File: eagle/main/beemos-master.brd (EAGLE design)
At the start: 99.1 x 73.7 mm, 50 parts, among them CON1 BAT, CON2 JACK_DC_BARREL, CON3 SPI, IC1 32U4, IC2 MCP73831T, IC3 MCP1703CB, IC4 DMP1045U, J1 RJ123.3, J10 RJ12STRAIGHT-I2C, J2 RJ123.3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

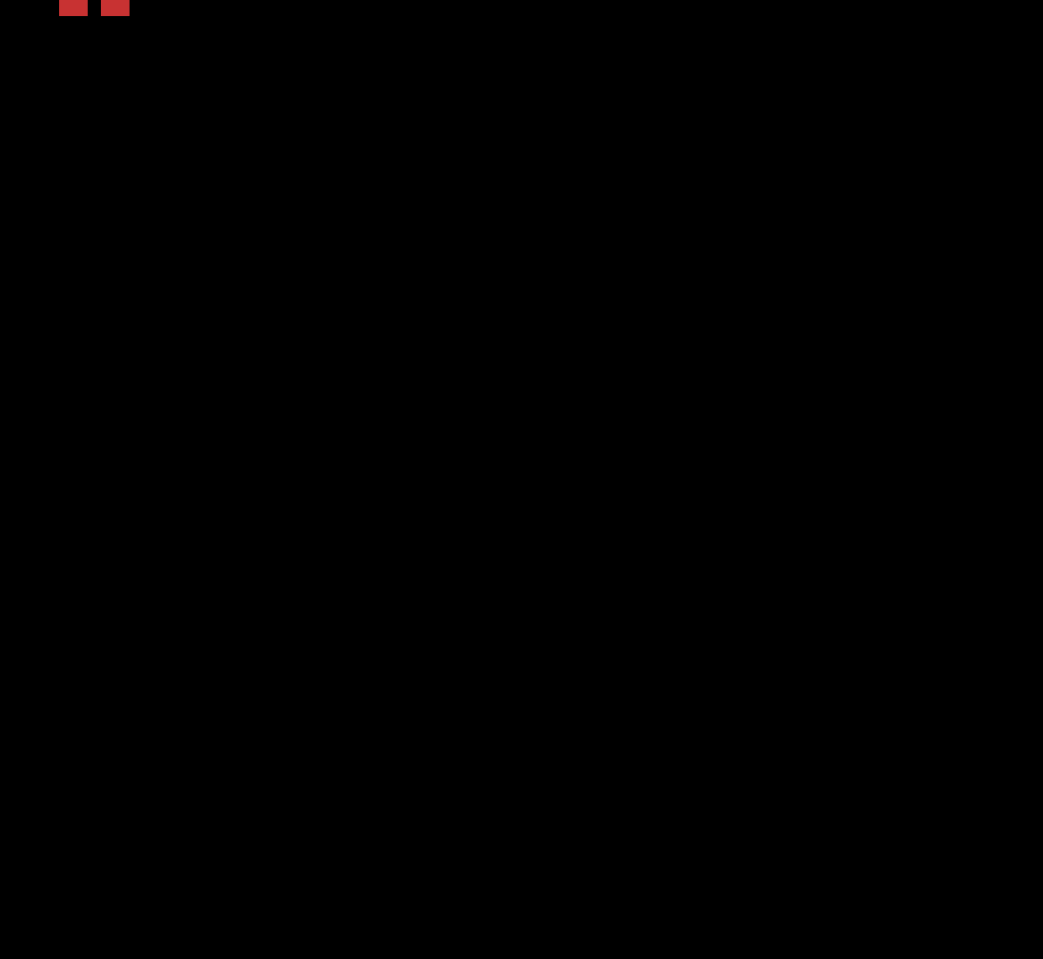
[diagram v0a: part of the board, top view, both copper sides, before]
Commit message: Added modules to schematics
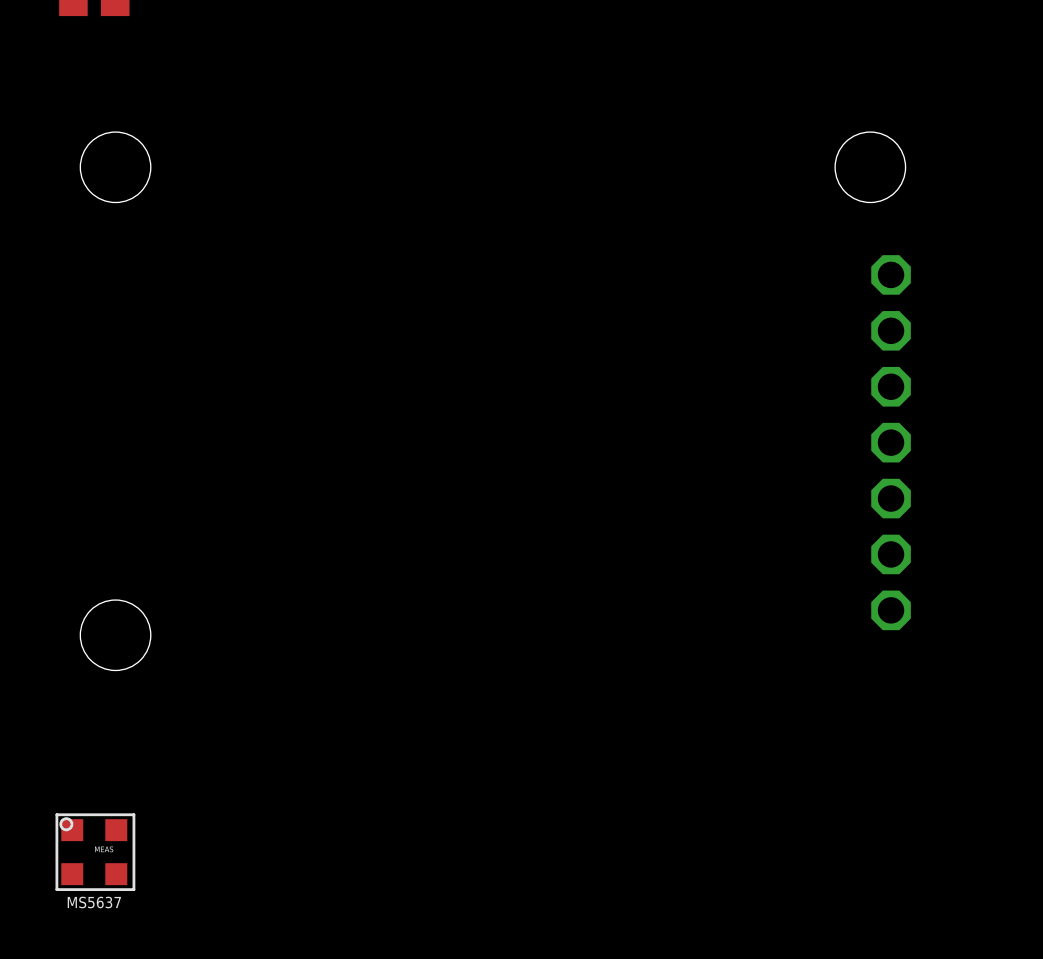
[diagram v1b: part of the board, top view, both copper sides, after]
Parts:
- added U$6: SIM800L, SIM800L:SIP
- added U$7: MS5637, MS5637:MS5637
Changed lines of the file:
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@@
 <attribute name="LCSC" value="C17561" x="15.875" y="38.735" size="1.778" layer="27" rot="R180" display="off"/>
 <attribute name="NAME" x="13.094346875" y="39.39859375" size="1.27" layer="25" rot="R180"/>
+<attribute name="SPICEPREFIX" value="R" x="15.875" y="38.735" size="1.778" layer="27" rot="R180" display="off"/>
 <attribute name="VALUE" x="17.181590625" y="42.674859375" size="1.27" layer="27" rot="R180"/>
 </element>
@@
 <attribute name="LCSC" value="C17407" x="74.93" y="38.4429" size="1.778" layer="27" rot="R90" display="off"/>
 <attribute name="MPN" value="RC1206FR-07100KL" x="74.93" y="38.4429" size="1.778" layer="27" rot="R90" display="off"/>
+<attribute name="SPICEPREFIX" value="R" x="74.93" y="38.4429" size="1.778" layer="27" rot="R90" display="off"/>
 </element>
 <element name="CON1" library="jumper" library_urn="urn:adsk.eagle:library:252" package="JP1" package3d_urn="urn:adsk.eagle:package:15455/1" value="BAT" x="34.29" y="62.23" rot="R90"/>
@@
 <element name="CON2" library="lpatiny" package="DC_BARREL" value="JACK_DC_BARREL" x="-0.635" y="22.225" rot="R270"/>
 <element name="J8" library="lpatiny" package="RJ12-STRAIGHT-3.3" value="RJ123.3" x="49.53" y="12.065" rot="MR180"/>
-<element name="LDR" library="rcl" library_urn="urn:adsk.eagle:library:334" package="0207/2V" package3d_urn="urn:adsk.eagle:package:23490/1" value="" x="5.715" y="-10.16"/>
+<element name="LDR" library="rcl" library_urn="urn:adsk.eagle:library:334" package="0207/2V" package3d_urn="urn:adsk.eagle:package:23490/1" value="" x="5.715" y="-10.16">
+<attribute name="SPICEPREFIX" value="R" x="5.715" y="-10.16" size="1.778" layer="27" display="off"/>
+</element>
 <element name="R2" library="rcl" library_urn="urn:adsk.eagle:library:334" package="R0805" package3d_urn="urn:adsk.eagle:package:23553/2" value="10k" x="0" y="-19.685">
 <attribute name="ELECROW" value="C17407" x="0" y="-19.685" size="1.778" layer="27" display="off"/>
 <attribute name="LCSC" value="C17407" x="0" y="-19.685" size="1.778" layer="27" display="off"/>
 <attribute name="MPN" value="RC1206FR-07100KL" x="0" y="-19.685" size="1.778" layer="27" display="off"/>
+<attribute name="SPICEPREFIX" value="R" x="0" y="-19.685" size="1.778" layer="27" display="off"/>
 </element>
 <element name="D4" library="diode" library_urn="urn:adsk.eagle:library:210" package="SOD123" package3d_urn="urn:adsk.eagle:package:43420/1" value="Schottky" x="2.54" y="-26.035">
@@
 <element name="R1" library="rcl" package="R0805" value="4.7k" x="-11.43" y="-57.15"/>
 <element name="R6" library="rcl" package="R0805" value="4.7k" x="-11.43" y="-63.5"/>
+<element name="U$6" library="SIM800L" package="SIP" value="SIM800L" x="-13.335" y="-95.25"/>
+<element name="U$7" library="MS5637" package="MS5637" value="MS5637" x="-11.43" y="-102.235"/>
 </elements>
 <signals>

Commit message: Placed SIM800L module, added connections in schematic
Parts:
- removed C12: 10u, rcl:C0805K
- removed C13: 100nF, rcl:C0805K
- removed LDR: (no value), rcl:0207/2V
- removed R2: 10k, rcl:R0805
- removed U$7: MS5637, MS5637:MS5637
- moved U$6 159.1 mm to (94.0, 22.2), flipped to the bottom
- moved D4 60.9 mm to (23.5, 31.1)
- moved CON3 29.1 mm to (84.5, 17.8)
- moved C9 4.07 mm to (62.5, 31.8)
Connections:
- removed net SCL1: J1.SCL, J5.SCL
- removed net SCL2: J2.SCL
- removed net SCL3: J3.SCL, J6.SCL
- removed net SCL4: J4.SCL
- removed net SDA1: J1.SDA, J5.SDA
- removed net SDA2: J2.SDA
- removed net SDA3: J3.SDA, J6.SDA
- removed net SDA4: J4.SDA
- net 3.3V: now also U$6.7
- net A5: no longer LDR.2, R2.2
- net D14: no longer C12.1, C13.1, R2.1
- net GND: now also U$6.2, U$6.6; no longer C12.2, C13.2, LDR.1
- net RX: now also U$6.4
- net SCL: now also J1.SCL, J2.SCL, J3.SCL, J4.SCL, J5.SCL, J6.SCL
- net SDA: now also J1.SDA, J2.SDA, J3.SDA, J4.SDA, J5.SDA, J6.SDA
- net TX: now also U$6.5
- net VBAT1: now also U$6.3
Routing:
- net 3.3V: track 105.6 -> 260.2 mm
- net ISP+5V: track 0.00 -> 115.5 mm, vias 0 -> 2
- net MOSI: track 0.00 -> 38.5 mm, vias 0 -> 2
- net SCK: track 0.00 -> 32.8 mm, vias 0 -> 2
- net MISO: track 0.00 -> 30.1 mm, vias 0 -> 2
- net N$3: track 0.00 -> 20.5 mm, vias 0 -> 2
- net RESET: track 10.5 -> 20.0 mm
- net N$15: track 61.1 -> 66.2 mm
- net N$1: track 7.73 -> 6.56 mm
- net GND: track 212.5 -> 212.2 mm, vias 19 -> 21
